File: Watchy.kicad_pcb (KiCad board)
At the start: 2 copper layers, 33.8 x 46 mm, 67 parts, among them J1 FPC24(0.5MM), J2 USB_C_Receptacle_USB2.0, J3 Battery, M1 Vibration_Motor, Q1 AO3400A, Q2 UMH3N, Q4 CJ2301, Q5 S8050, SW1 BTN, SW2 BTN, SW3 BTN, SW4 BTN, U1 ESP32-PICO-D4, U2 ME6211C33M5G-N, U3 CP2102, U4 BMA423, U5 TP4054, U6 PCF8563BS, Y1 32.768KHz

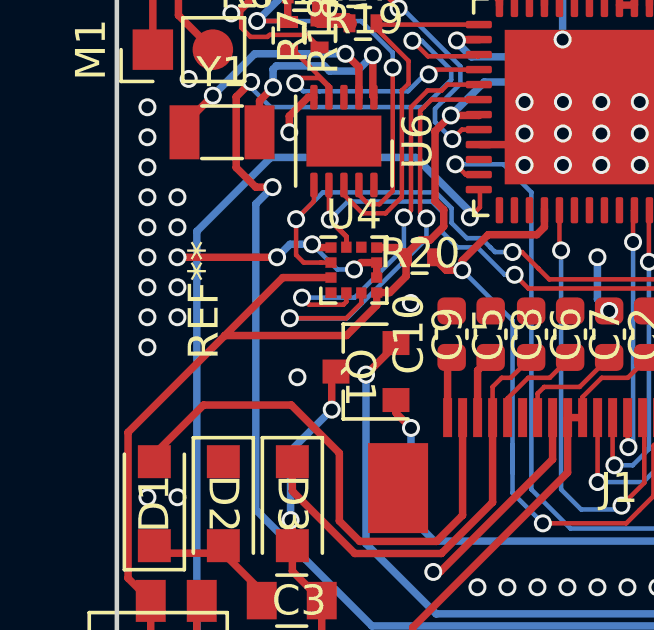
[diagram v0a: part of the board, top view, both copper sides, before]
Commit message: add most 3d models
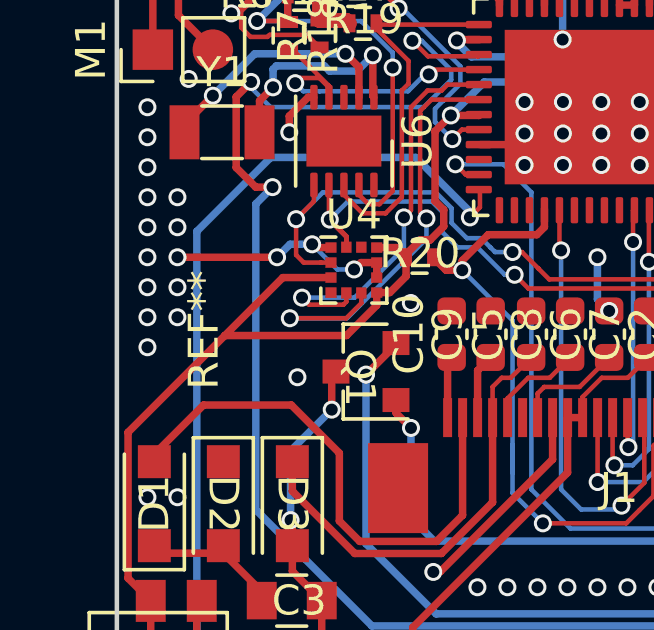
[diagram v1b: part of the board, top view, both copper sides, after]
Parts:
- moved REF** 1.00 mm to (72.1, 94.5)
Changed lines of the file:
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@@
     (pad "3" smd rect (at 1 0 90) (size 0.9 0.8) (layers "F.Cu" "F.Paste" "F.Mask")
       (net 27 "+BATT") (pinfunction "D") (pintype "passive"))
+    (model "${KICAD6_3DMODEL_DIR}/Package_TO_SOT_SMD.3dshapes/SOT-23.wrl"
+      (offset (xyz 0 0 0))
+      (scale (xyz 1 1 1))
+      (rotate (xyz 0 0 0))
+    )
   )
   (footprint "Watchy:SOT-23" (layer "F.Cu")
@@
     (pad "3" smd rect (at 1 0 180) (size 0.9 0.8) (layers "F.Cu" "F.Paste" "F.Mask")
       (net 41 "Net-(D6-A)") (pinfunction "C") (pintype "passive"))
+    (model "${KICAD6_3DMODEL_DIR}/Package_TO_SOT_SMD.3dshapes/SOT-23.wrl"
+      (offset (xyz 0 0 0))
+      (scale (xyz 1 1 1))
+      (rotate (xyz 0 0 0))
+    )
   )
   (footprint "Watchy:R_0402" (layer "F.Cu")
@@
     (pad "3" smd rect (at 1 0 180) (size 0.9 0.8) (layers "F.Cu" "F.Paste" "F.Mask")
       (net 18 "Net-(D3-A)") (pinfunction "D") (pintype "passive"))
+    (model "${KICAD6_3DMODEL_DIR}/Package_TO_SOT_SMD.3dshapes/SOT-23.wrl"
+      (offset (xyz 0 0 0))
+      (scale (xyz 1 1 1))
+      (rotate (xyz 0 0 0))
+    )
   )
   (footprint "Inductor_SMD:L_Taiyo-Yuden_NR-40xx" (layer "F.Cu")
@@
     (property "ki_keywords" "inductor choke coil reactor magnetic")
     (attr smd)
-    (fp_text reference "L1" (at 0 -3 -90) (layer "F.SilkS")
+    (fp_text reference "L1" (at 0 -3 90) (layer "F.SilkS")
         (effects (font (size 1 1) (thickness 0.15)))
     )
-    (fp_text value "10uH 1A" (at 0 3.5 -90) (layer "F.Fab")
+    (fp_text value "10uH 1A" (at 0 3.5 90) (layer "F.Fab")
         (effects (font (size 1 1) (thickness 0.15)))
     )
-    (fp_text user "${REFERENCE}" (at 0 0 -90) (layer "F.Fab")
+    (fp_text user "${REFERENCE}" (at 0 0 90) (layer "F.Fab")
         (effects (font (size 1 1) (thickness 0.15)))
     )
@@
     (pad "2" smd rect (at 1.4 0 270) (size 1.1 1.1) (layers "F.Cu" "F.Paste" "F.Mask")
       (net 18 "Net-(D3-A)") (pinfunction "A") (pintype "passive"))
+    (model "${KICAD6_3DMODEL_DIR}/Diode_SMD.3dshapes/D_SOD-123.wrl"
+      (offset (xyz 0 0 0))
+      (scale (xyz 1 1 1))
+      (rotate (xyz 0 0 0))
+    )
   )
   (footprint "Package_DFN_QFN:QFN-48-1EP_7x7mm_P0.5mm_EP5.15x5.15mm" (layer "F.Cu")
@@
     (pad "2" smd rect (at 1 0) (size 1 1.25) (layers "F.Cu" "F.Paste" "F.Mask")
       (net 1 "GND") (pintype "passive"))
+    (model "${KICAD6_3DMODEL_DIR}/Capacitor_SMD.3dshapes/C_0805_2012Metric.wrl"
+      (offset (xyz 0 0 0))
+      (scale (xyz 1 1 1))
+      (rotate (xyz 0 0 0))
+    )
   )
   (footprint "Watchy:R_0402" (layer "F.Cu")
@@
     (pad "2" smd rect (at 1.4 0 270) (size 1.1 1.1) (layers "F.Cu" "F.Paste" "F.Mask")
       (net 17 "Net-(D1-K)") (pinfunction "A") (pintype "passive"))
+    (model "${KICAD6_3DMODEL_DIR}/Diode_SMD.3dshapes/D_SOD-123.wrl"
+      (offset (xyz 0 0 0))
+      (scale (xyz 1 1 1))
+      (rotate (xyz 0 0 0))
+    )
   )
   (footprint "Watchy:C_0805" (layer "F.Cu")
@@
     (pad "2" smd rect (at 1 0) (size 1 1.25) (layers "F.Cu" "F.Paste" "F.Mask")
       (net 18 "Net-(D3-A)") (pintype "passive"))
+    (model "${KICAD6_3DMODEL_DIR}/Capacitor_SMD.3dshapes/C_0805_2012Metric.wrl"
+      (offset (xyz 0 0 0))
+      (scale (xyz 1 1 1))
+      (rotate (xyz 0 0 0))
+    )
   )
   (footprint "Watchy:R_0402" (layer "F.Cu")
@@
     (pad "2" smd rect (at 0.8 0 270) (size 0.8 0.8) (layers "F.Cu" "F.Paste" "F.Mask")
       (net 6 "VBUS") (pinfunction "A") (pintype "passive"))
+    (model "${KICAD6_3DMODEL_DIR}/LED_SMD.3dshapes/LED_0603_1608Metric.wrl"
+      (offset (xyz 0 0 0))
+      (scale (xyz 1 1 1))
+      (rotate (xyz 0 0 0))
+    )
   )
   (footprint "Watchy:C_0805" (layer "F.Cu")
@@
     (pad "2" smd rect (at 1 0) (size 1 1.25) (layers "F.Cu" "F.Paste" "F.Mask")
       (net 1 "GND") (pintype "passive"))
+    (model "${KICAD6_3DMODEL_DIR}/Capacitor_SMD.3dshapes/C_0805_2012Metric.wrl"
+      (offset (xyz 0 0 0))
+      (scale (xyz 1 1 1))
+      (rotate (xyz 0 0 0))
+    )
   )
   (footprint "Watchy:D_SOD-123" (layer "F.Cu")
@@
     (pad "2" smd rect (at 1.4 0 180) (size 1.1 1.1) (layers "F.Cu" "F.Paste" "F.Mask")
       (net 6 "VBUS") (pinfunction "A") (pintype "passive"))
+    (model "${KICAD6_3DMODEL_DIR}/Diode_SMD.3dshapes/D_SOD-123.wrl"
+      (offset (xyz 0 0 0))
+      (scale (xyz 1 1 1))
+      (rotate (xyz 0 0 0))
+    )
   )
   (footprint "Package_TO_SOT_SMD:SOT-23-5" (layer "F.Cu")
@@
     (pad "2" smd rect (at 0.625 2.9 90) (size 0.5 1.6) (layers "F.Cu" "F.Paste" "F.Mask")
       (net 1 "GND") (pinfunction "Pin_2") (pintype "passive"))
+    (model "${KIPRJMOD}/3D/Molex_PicoBlade_53261-0271_1x02-1MP_P1.25mm_Horizontal.step"
+      (offset (xyz 0 -0.5 0))
+      (scale (xyz 1 1 1))
+      (rotate (xyz 0 0 180))
+    )
   )
   (footprint "Watchy:D_SOD-123" (layer "F.Cu")
@@
     (pad "2" smd rect (at 1.4 0 90) (size 1.1 1.1) (layers "F.Cu" "F.Paste" "F.Mask")
       (net 5 "PREVGL") (pinfunction "A") (pintype "passive"))
+    (model "${KICAD6_3DMODEL_DIR}/Diode_SMD.3dshapes/D_SOD-123.wrl"
+      (offset (xyz 0 0 0))
+      (scale (xyz 1 1 1))
+      (rotate (xyz 0 0 0))
+    )
   )
   (footprint "Watchy:SOT-23-5" (layer "F.Cu")
@@
     (pad "5" smd rect (at 1.1 -0.95 90) (size 1.06 0.65) (layers "F.Cu" "F.Paste" "F.Mask")
       (net 3 "+3V3") (pinfunction "OUT") (pintype "power_out"))
+    (model "${KICAD6_3DMODEL_DIR}/Package_TO_SOT_SMD.3dshapes/SOT-23-5.wrl"
+      (offset (xyz 0 0 0))
+      (scale (xyz 1 1 1))
+      (rotate (xyz 0 0 0))
+    )
   )
   (footprint "Watchy:K2-1114SA-A4SW-06" locked (layer "F.Cu")
@@
     (pad "M" smd rect locked (at -7.4 0) (size 2 3) (layers "F.Cu" "F.Paste" "F.Mask"))
     (pad "M" smd rect locked (at 7.4 0) (size 2 3) (layers "F.Cu" "F.Paste" "F.Mask"))
+    (model "${KIPRJMOD}/3D/FPC-24.stp"
+      (offset (xyz -5.75 2.5 0))
+      (scale (xyz 1 1 1))
+      (rotate (xyz 0 0 0))
+    )
   )
   (footprint "Watchy:R_0402" (layer "F.Cu")
@@
     (pad "2" smd rect (at 1.4 0 270) (size 1.1 1.1) (layers "F.Cu" "F.Paste" "F.Mask")
       (net 41 "Net-(D6-A)") (pinfunction "A") (pintype "passive"))
+    (model "${KICAD6_3DMODEL_DIR}/Diode_SMD.3dshapes/D_SOD-123.wrl"
+      (offset (xyz 0 0 0))
+      (scale (xyz 1 1 1))
+      (rotate (xyz 0 0 0))
+    )
   )
   (footprint "Watchy:Motor_Header" (layer "F.Cu")
@@
       (net 96 "unconnected-(U6-NC-Pad10)") (pinfunction "NC") (pintype "no_connect"))
     (pad "11" smd rect (at 0 0 270) (size 1.7 2.5) (layers "F.Cu" "F.Mask"))
-    (model "${KICAD6_3DMODEL_DIR}/Package_DFN_QFN.3dshapes/DFN-10-1EP_3x3mm_P0.5mm_EP1.7x2.5mm.wrl"
+    (model "${KICAD7_3DMODEL_DIR}/Package_DFN_QFN.3dshapes/DFN-10-1EP_3x3mm_P0.5mm_EP1.75x2.7mm.wrl"
       (offset (xyz 0 0 0))
       (scale (xyz 1 1 1))
@@
   )
   (footprint "Watchy:VIB_MOT_LBM0625A3098" (layer "F.Cu")
-    (at 72.0984 93.5004 90)
+    (at 72.0984 94.5 90)
     (attr smd)
     (fp_text reference "REF**" (at 0 -0.5 90 unlocked) (layer "F.SilkS")
@@
     (fp_circle (center 0 0) (end 3 0)
       (stroke (width 0.12) (type default)) (fill none) (layer "Dwgs.User"))
+    (model "${KIPRJMOD}/3D/VIB_MOT.step"
+      (offset (xyz 0 0 0))
+      (scale (xyz 1 1 1))
+      (rotate (xyz 0 0 0))
+    )
   )
   (footprint "Watchy:R_0402" (layer "F.Cu")

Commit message: update clearances
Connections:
- C13 pad 1: Net-(U3-VDD) -> (no net)
- D4 pad 1: Net-(D4-K) -> (no net)
- Q4 pad 2: Net-(D4-K) -> (no net)
- U2 pad 1: Net-(D4-K) -> (no net)
- U2 pad 3: Net-(D4-K) -> (no net)
- U3 pad 5: Net-(U3-VDD) -> (no net)
- U3 pad 6: Net-(U3-VDD) -> (no net)
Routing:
- net (no net): track 0.00 -> 12.4 mm
- net Net-(D4-K): track 10.5 -> 0.00 mm
- net Net-(U3-VDD): track 1.91 -> 0.00 mm
- net GND: vias 174 -> 170

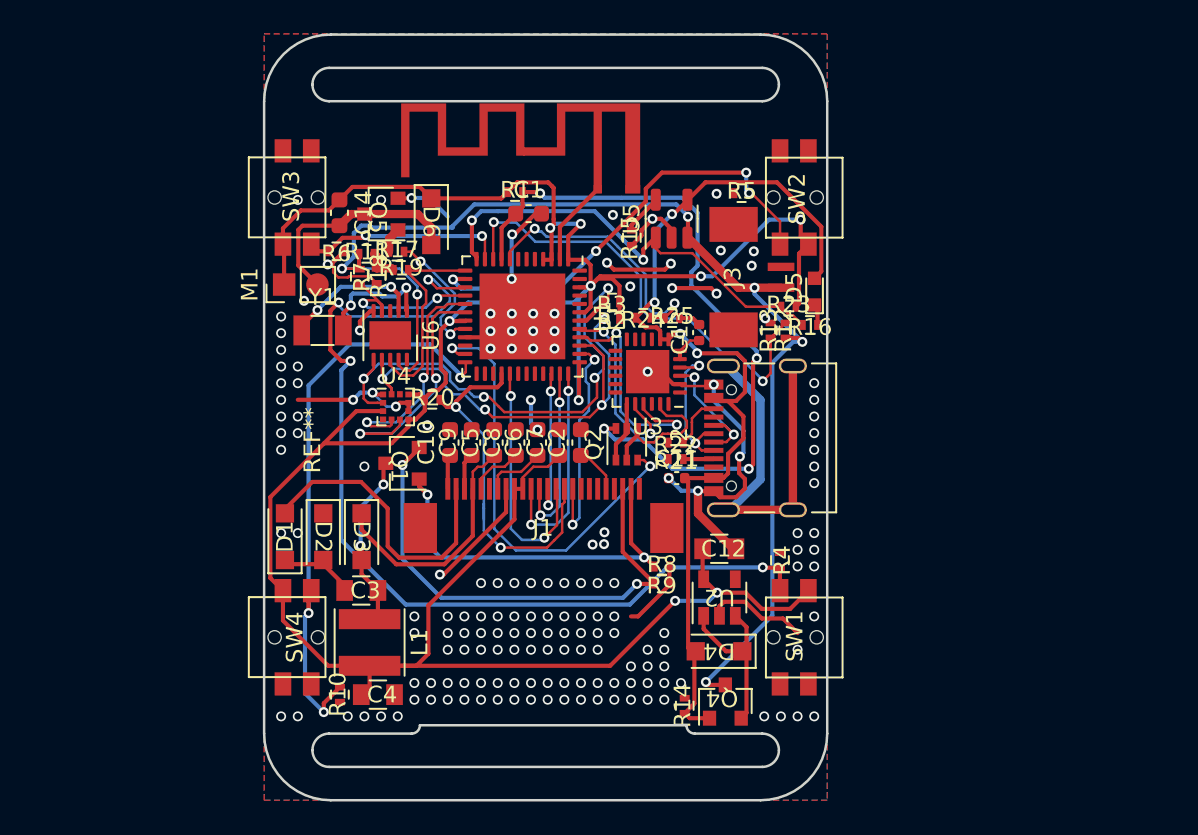
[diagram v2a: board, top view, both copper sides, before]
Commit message: update pcb to suite jlcpcb specs
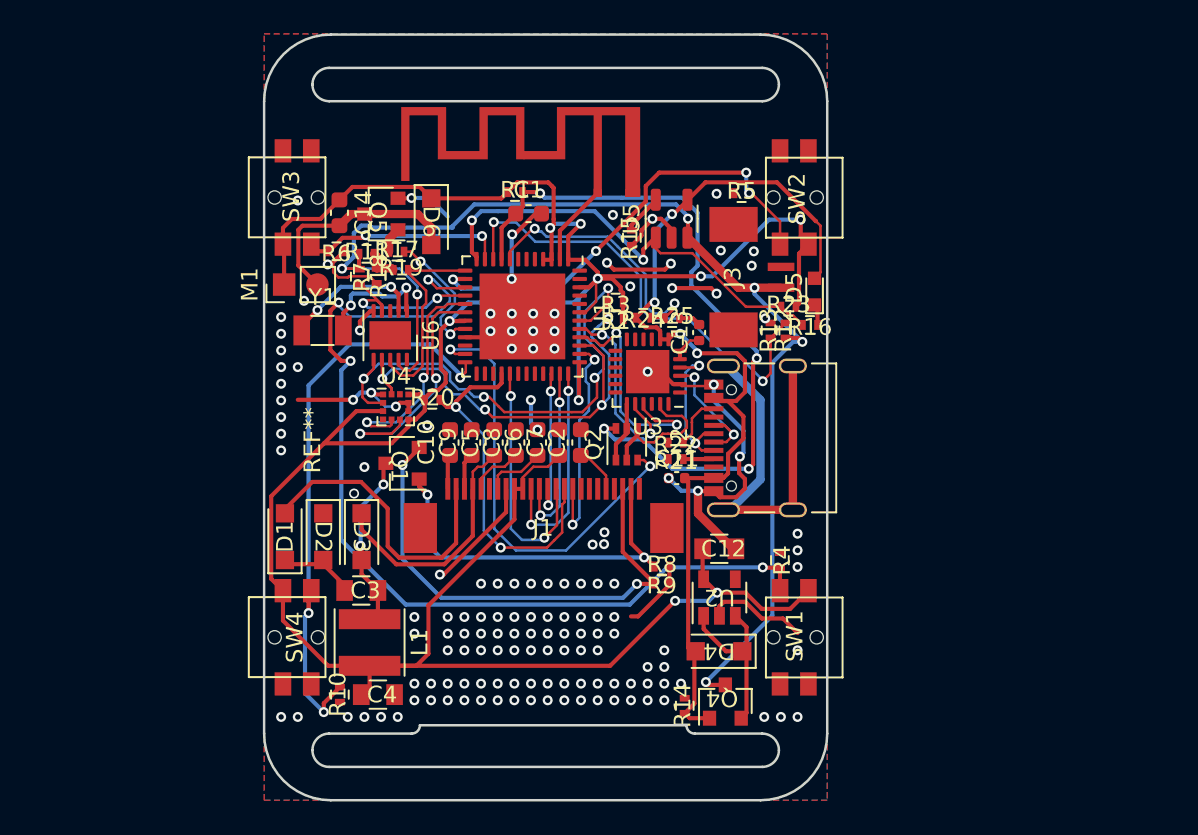
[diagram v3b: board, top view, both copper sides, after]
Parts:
- moved R2 0.22 mm to (89.8, 87.2)
- moved R3 0.22 mm to (89.8, 86.2)
- moved AE1 0.22 mm to (74.3, 79.4)
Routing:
- net RES: track 22.5 -> 21.6 mm
- net +3V3: track 171.5 -> 172.2 mm
- net GND: track 79.6 -> 79.7 mm, vias 170 -> 149

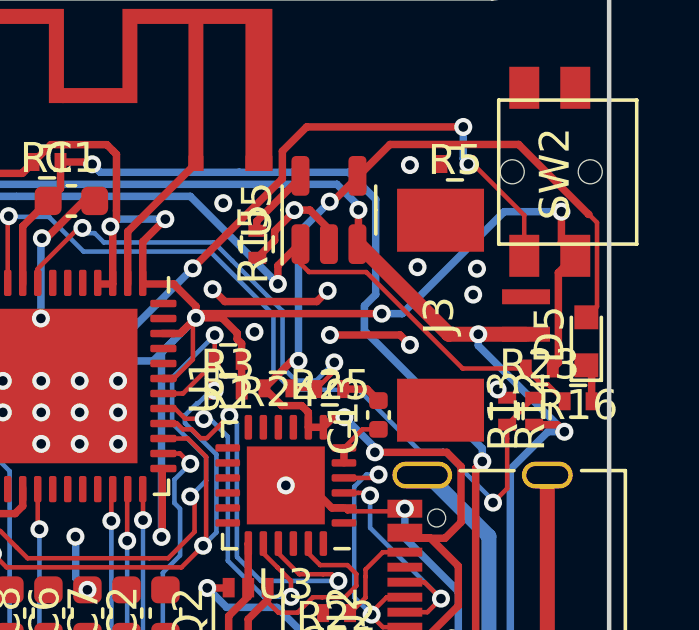
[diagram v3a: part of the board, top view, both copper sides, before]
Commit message: replace battery connector with pads
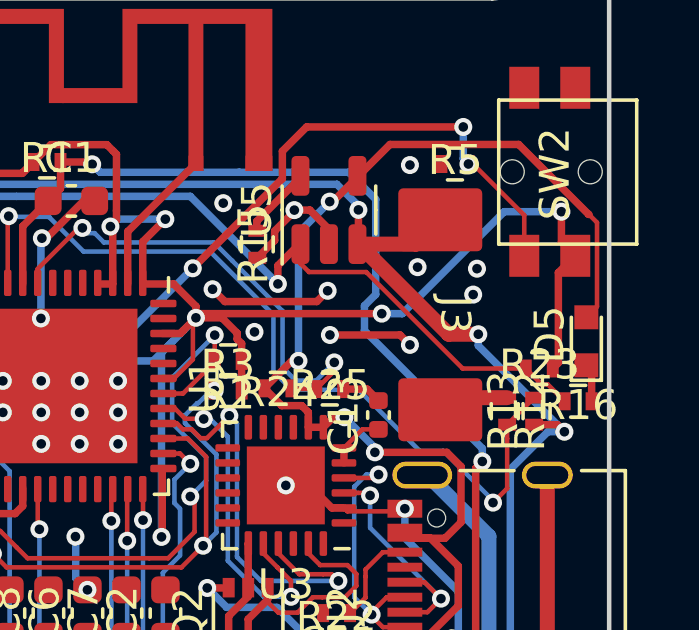
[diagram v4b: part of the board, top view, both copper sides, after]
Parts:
- AE1: value Val** -> SWRA117D
- J3: footprint Watchy:1.25T-2PWT (Molex 532610271) -> Watchy:BatteryPads
- turned J3 to -90 degrees
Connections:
- C13 pad 1: (no net) -> Net-(#FLG01-pwr)
- D4 pad 1: (no net) -> Net-(#FLG02-pwr)
- Q4 pad 2: (no net) -> Net-(#FLG02-pwr)
- U2 pad 1: (no net) -> Net-(#FLG02-pwr)
- U2 pad 3: (no net) -> Net-(#FLG02-pwr)
- U3 pad 5: (no net) -> Net-(#FLG01-pwr)
- U3 pad 6: (no net) -> Net-(#FLG01-pwr)
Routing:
- net (no net): track 12.4 -> 0.00 mm
- net Net-(#FLG02-pwr): track 0.00 -> 10.5 mm
- net GND: track 79.7 -> 82.7 mm, vias 149 -> 148
- net Net-(#FLG01-pwr): track 0.00 -> 1.91 mm
- net +BATT: track 75.1 -> 76.6 mm
